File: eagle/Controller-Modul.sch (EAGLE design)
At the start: 36 parts, among them IC3 ATMEGA328P, Q1 BC550C

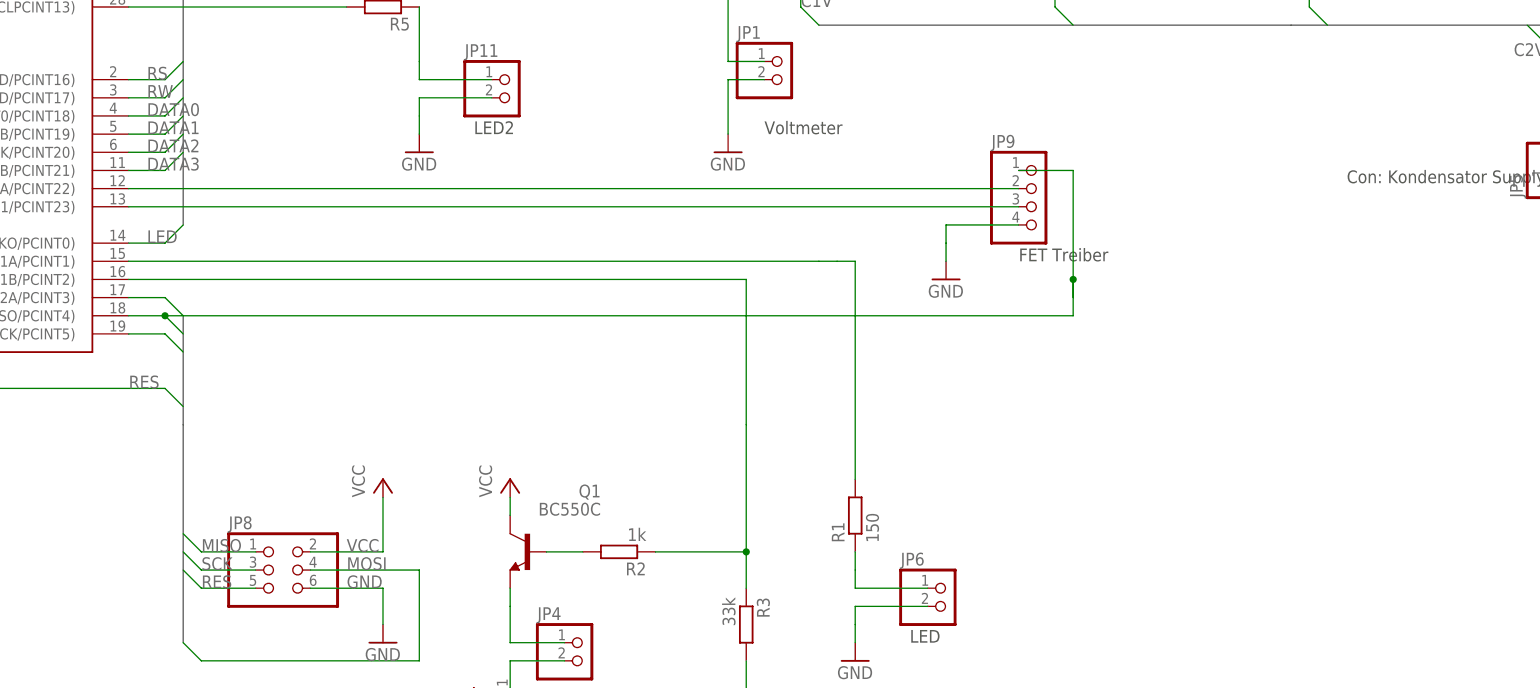
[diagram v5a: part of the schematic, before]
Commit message: Added forgotten Pull-Down resistors. Lots of new code for executing mosfets
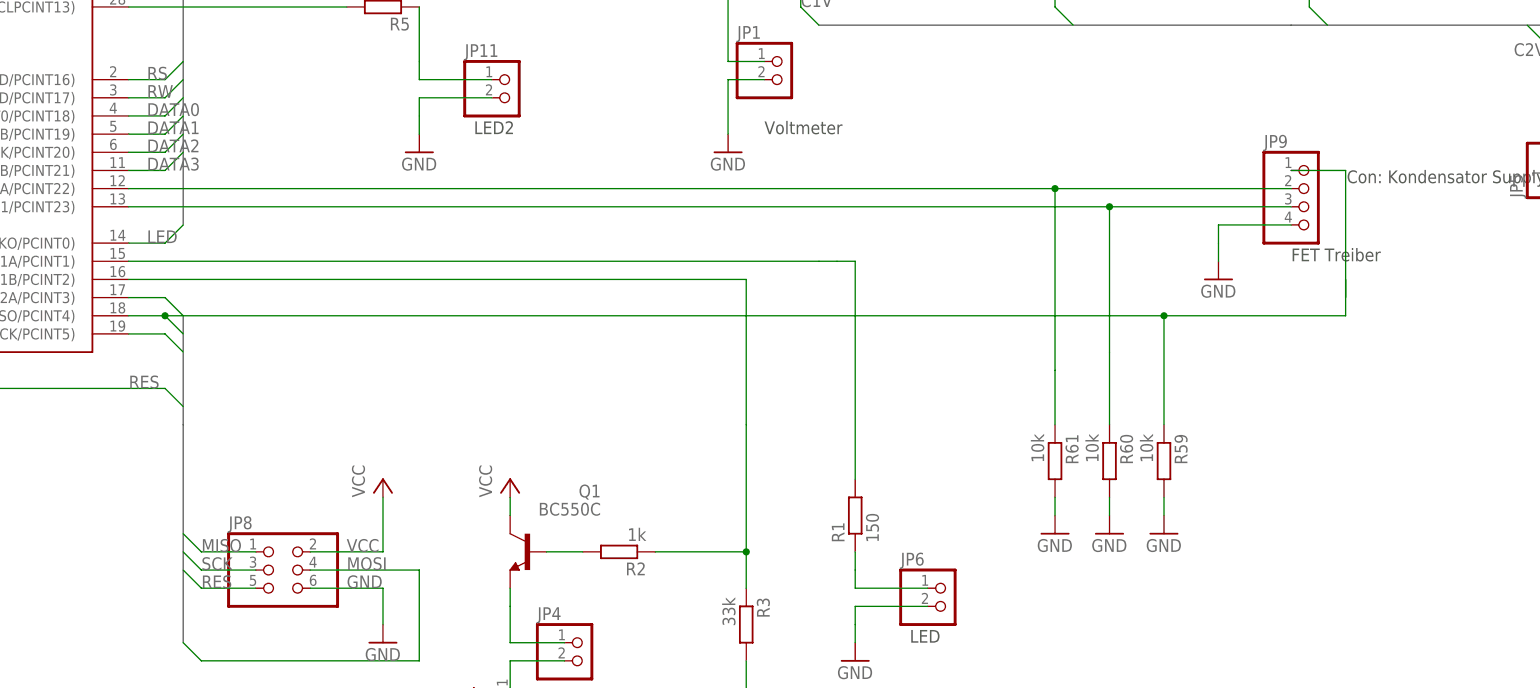
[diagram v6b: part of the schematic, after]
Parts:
- added R59, R60, R61: 10k, resistor:R-EU_R1206
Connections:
- removed net N$31: IC3.PD7(AIN1/PCINT23), JP9.3
- removed net N$34: IC3.PD6(AIN0/OC0A/PCINT22), JP9.2
- new net FET2: IC3.PD7(AIN1/PCINT23), JP9.3, R60.1
- new net FET3: IC3.PD6(AIN0/OC0A/PCINT22), JP9.2, R61.1
- net GND: now also R59.2, R60.2, R61.2
- net MISO: now also R59.1
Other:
- moved on the sheet: JP9
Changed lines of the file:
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@@
 <part name="R16" library="resistor" deviceset="R-EU_" device="R1206" value="3k9"/>
 <part name="GND5" library="supply1" deviceset="GND" device=""/>
+<part name="R59" library="resistor" deviceset="R-EU_" device="R1206" value="10k"/>
+<part name="R60" library="resistor" deviceset="R-EU_" device="R1206" value="10k"/>
+<part name="R61" library="resistor" deviceset="R-EU_" device="R1206" value="10k"/>
+<part name="GND57" library="supply1" deviceset="GND" device=""/>
+<part name="GND58" library="supply1" deviceset="GND" device=""/>
+<part name="GND59" library="supply1" deviceset="GND" device=""/>
 </parts>
 <sheets>
@@
 <text x="167.64" y="55.88" size="1.778" layer="97">Fußtaster</text>
 <text x="144.78" y="53.34" size="1.778" layer="97">AutoSchalter</text>
-<text x="248.92" y="2.54" size="1.778" layer="97">FET Treiber</text>
+<text x="287.02" y="2.54" size="1.778" layer="97">FET Treiber</text>
 <text x="172.72" y="20.32" size="1.778" layer="97">LED2</text>
 </plain>
@@
 <instance part="JP1" gate="G$1" x="215.9" y="27.94"/>
 <instance part="GND6" gate="1" x="208.28" y="17.78"/>
-<instance part="JP9" gate="A" x="251.46" y="10.16"/>
-<instance part="GND2" gate="1" x="238.76" y="0"/>
+<instance part="JP9" gate="A" x="289.56" y="10.16"/>
+<instance part="GND2" gate="1" x="276.86" y="0"/>
 <instance part="R5" gate="G$1" x="160.02" y="38.1" rot="R180"/>
 <instance part="GND1" gate="1" x="165.1" y="17.78"/>
@@
 <instance part="R16" gate="G$1" x="289.56" y="53.34" rot="R90"/>
 <instance part="GND5" gate="1" x="297.18" y="68.58"/>
+<instance part="R59" gate="G$1" x="269.24" y="-25.4" rot="R270"/>
+<instance part="R60" gate="G$1" x="261.62" y="-25.4" rot="R270"/>
+<instance part="R61" gate="G$1" x="254" y="-25.4" rot="R270"/>
+<instance part="GND57" gate="1" x="254" y="-35.56"/>
+<instance part="GND58" gate="1" x="261.62" y="-35.56"/>
+<instance part="GND59" gate="1" x="269.24" y="-35.56"/>
 </instances>
 <busses>
@@
 <segment>
 <pinref part="JP9" gate="A" pin="4"/>
-<wire x1="248.92" y1="7.62" x2="238.76" y2="7.62" width="0.1524" layer="91"/>
-<wire x1="238.76" y1="7.62" x2="238.76" y2="5.08" width="0.1524" layer="91"/>
-<wire x1="238.76" y1="5.08" x2="238.76" y2="2.54" width="0.1524" layer="91"/>
+<wire x1="287.02" y1="7.62" x2="276.86" y2="7.62" width="0.1524" layer="91"/>
+<wire x1="276.86" y1="7.62" x2="276.86" y2="5.08" width="0.1524" layer="91"/>
+<wire x1="276.86" y1="5.08" x2="276.86" y2="2.54" width="0.1524" layer="91"/>
 <pinref part="GND2" gate="1" pin="GND"/>
 </segment>
@@
 <wire x1="274.32" y1="78.74" x2="274.32" y2="73.66" width="0.1524" layer="91"/>
 </segment>
+<segment>
+<pinref part="R61" gate="G$1" pin="2"/>
+<pinref part="GND57" gate="1" pin="GND"/>
+<wire x1="254" y1="-30.48" x2="254" y2="-33.02" width="0.1524" layer="91"/>
+</segment>
+<segment>
+<pinref part="R60" gate="G$1" pin="2"/>
+<pinref part="GND58" gate="1" pin="GND"/>
+<wire x1="261.62" y1="-30.48" x2="261.62" y2="-33.02" width="0.1524" layer="91"/>
+</segment>
+<segment>
+<pinref part="R59" gate="G$1" pin="2"/>
+<pinref part="GND59" gate="1" pin="GND"/>
+<wire x1="269.24" y1="-30.48" x2="269.24" y2="-33.02" width="0.1524" layer="91"/>
+</segment>
 </net>
 <net name="N$6" class="0">
@@
 <pinref part="IC3" gate="1" pin="PB4(MISO/PCINT4)"/>
 <wire x1="129.54" y1="-5.08" x2="124.46" y2="-5.08" width="0.1524" layer="91"/>
-<wire x1="256.54" y1="-2.54" x2="256.54" y2="0" width="0.1524" layer="91"/>
 <pinref part="JP9" gate="A" pin="1"/>
-<wire x1="256.54" y1="0" x2="256.54" y2="15.24" width="0.1524" layer="91"/>
-<wire x1="256.54" y1="15.24" x2="248.92" y2="15.24" width="0.1524" layer="91"/>
-<wire x1="129.54" y1="-5.08" x2="256.54" y2="-5.08" width="0.1524" layer="91"/>
-<wire x1="256.54" y1="-5.08" x2="256.54" y2="0" width="0.1524" layer="91"/>
+<wire x1="294.64" y1="-5.08" x2="294.64" y2="15.24" width="0.1524" layer="91"/>
+<wire x1="294.64" y1="15.24" x2="287.02" y2="15.24" width="0.1524" layer="91"/>
+<wire x1="129.54" y1="-5.08" x2="269.24" y2="-5.08" width="0.1524" layer="91"/>
+<wire x1="269.24" y1="-5.08" x2="294.64" y2="-5.08" width="0.1524" layer="91"/>
 <junction x="129.54" y="-5.08"/>
-<junction x="256.54" y="0"/>
+<pinref part="R59" gate="G$1" pin="1"/>
+<wire x1="269.24" y1="-5.08" x2="269.24" y2="-20.32" width="0.1524" layer="91"/>
+<junction x="269.24" y="-5.08"/>
 </segment>
 </net>
@@
 <pinref part="R1" gate="G$1" pin="2"/>
 <wire x1="226.06" y1="2.54" x2="226.06" y2="-27.94" width="0.1524" layer="91"/>
-</segment>
-</net>
-<net name="N$31" class="0">
-<segment>
-<pinref part="IC3" gate="1" pin="PD7(AIN1/PCINT23)"/>
-<wire x1="124.46" y1="10.16" x2="248.92" y2="10.16" width="0.1524" layer="91"/>
-<pinref part="JP9" gate="A" pin="3"/>
-</segment>
-</net>
-<net name="N$34" class="0">
-<segment>
-<pinref part="IC3" gate="1" pin="PD6(AIN0/OC0A/PCINT22)"/>
-<wire x1="124.46" y1="12.7" x2="248.92" y2="12.7" width="0.1524" layer="91"/>
-<pinref part="JP9" gate="A" pin="2"/>
 </segment>
 </net>
@@
 </segment>
 </net>
+<net name="FET2" class="0">
+<segment>
+<pinref part="R60" gate="G$1" pin="1"/>
+<wire x1="261.62" y1="-10.16" x2="261.62" y2="-20.32" width="0.1524" layer="91"/>
+<pinref part="IC3" gate="1" pin="PD7(AIN1/PCINT23)"/>
+<wire x1="124.46" y1="10.16" x2="261.62" y2="10.16" width="0.1524" layer="91"/>
+<pinref part="JP9" gate="A" pin="3"/>
+<wire x1="261.62" y1="10.16" x2="287.02" y2="10.16" width="0.1524" layer="91"/>
+<wire x1="261.62" y1="-10.16" x2="261.62" y2="10.16" width="0.1524" layer="91"/>
+<junction x="261.62" y="10.16"/>
+</segment>
+</net>
+<net name="FET3" class="0">
+<segment>
+<pinref part="R61" gate="G$1" pin="1"/>
+<wire x1="254" y1="-12.7" x2="254" y2="-20.32" width="0.1524" layer="91"/>
+<pinref part="IC3" gate="1" pin="PD6(AIN0/OC0A/PCINT22)"/>
+<wire x1="124.46" y1="12.7" x2="254" y2="12.7" width="0.1524" layer="91"/>
+<pinref part="JP9" gate="A" pin="2"/>
+<wire x1="254" y1="12.7" x2="287.02" y2="12.7" width="0.1524" layer="91"/>
+<wire x1="254" y1="-12.7" x2="254" y2="12.7" width="0.1524" layer="91"/>
+<junction x="254" y="12.7"/>
+</segment>
+</net>
+<net name="N$8" class="0">
+<segment>
+<wire x1="294.64" y1="-2.54" x2="294.64" y2="0" width="0.1524" layer="91"/>
+</segment>
+</net>
